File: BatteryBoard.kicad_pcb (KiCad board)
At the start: 4 copper layers, 124 parts, among them J1 Keystone-1042, J10 200528-0100, J2 Keystone-1042, J3 Keystone-1042, J4 Keystone-1042, J5 Keystone-1042, J6 Keystone-1042, J7 1824543, J8 Conn_01x06, Q1 NX3008NBKS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

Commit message: Repoured polys
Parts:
- moved U9 0.48 mm to (153.3, 98.5)
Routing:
- net SYSTEM_VDD: track 44.3 -> 36.3 mm
- net /Battery Bus Detection/CHARGE_EN: track 21.5 -> 20.7 mm
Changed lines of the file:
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@@
 	(footprint "Package_TO_SOT_SMD:TSOT-23-6"
 		(layer "B.Cu")
-		(at 153.3 98.01875 90)
+		(at 153.3 98.5 90)
 		(descr "TSOT, 6 Pin (https://www.jedec.org/sites/default/files/docs/MO-193D.pdf variant AA), generated with kicad-footprint-generator ipc_gullwing_generator.py")
 		(tags "TSOT TO_SOT_SMD")
@@
 	)
 	(segment
-		(start 154.25 96.88125)
-		(end 154.25 96.218751)
-		(width 0.381)
-		(layer "B.Cu")
-		(net 20)
-	)
-	(segment
 		(start 121.55 101.7125)
 		(end 121.8375 102)
@@
 	)
 	(segment
-		(start 154.25 96.218751)
-		(end 153.341999 95.31075)
-		(width 0.381)
-		(layer "B.Cu")
-		(net 20)
-	)
-	(segment
-		(start 149.299249 95.31075)
-		(end 147.885 96.724999)
-		(width 0.381)
-		(layer "B.Cu")
-		(net 20)
-	)
-	(segment
 		(start 121.5 114.0825)
 		(end 121.8375 114.42)
@@
 	)
 	(segment
-		(start 153.341999 95.31075)
-		(end 149.299249 95.31075)
-		(width 0.381)
-		(layer "B.Cu")
-		(net 20)
-	)
-	(segment
 		(start 121.55 98.25)
 		(end 121.55 101.7125)
@@
 	)
 	(segment
-		(start 150.051749 95.82825)
-		(end 153.07825 95.82825)
+		(start 153.3 97.20517)
+		(end 153.3 96.88125)
 		(width 0.254)
 		(layer "B.Cu")
@@
 	)
 	(segment
-		(start 153.07825 95.82825)
-		(end 153.3 96.05)
+		(start 153.3 97.68642)
+		(end 152.50517 98.48125)
 		(width 0.254)
 		(layer "B.Cu")
@@
 	)
 	(segment
-		(start 149.155 96.724999)
-		(end 150.051749 95.82825)
+		(start 152.50517 98.48125)
+		(end 150.911251 98.48125)
 		(width 0.254)
 		(layer "B.Cu")
@@
 	)
 	(segment
-		(start 153.3 96.05)
-		(end 153.3 96.88125)
+		(start 150.911251 98.48125)
+		(end 149.155 96.724999)
 		(width 0.254)
 		(layer "B.Cu")
@@
 	)
 	(segment
-		(start 144.825 107.825)
-		(end 143.5 107.825)
+		(start 155.614949 110.742999)
+		(end 145.742999 110.742999)
 		(width 0.254)
 		(layer "B.Cu")
@@
 	)
 	(segment
-		(start 143.75 107.825)
-		(end 143.075 107.825)
-		(width 0.381)
+		(start 143.5 108.5)
+		(end 143.5 107.825)
+		(width 0.254)
 		(layer "B.Cu")
 		(net 77)
 	)
 	(segment
-		(start 145.5 108.5)
-		(end 144.825 107.825)
+		(start 156.182949 110.174999)
+		(end 155.614949 110.742999)
 		(width 0.254)
 		(layer "B.Cu")
@@
 	)
 	(segment
-		(start 155.614949 110.742999)
-		(end 145.742999 110.742999)
-		(width 0.254)
-		(layer "B.Cu")
-		(net 77)
-	)
-	(segment
-		(start 145.5 110.5)
-		(end 145.5 108.5)
-		(width 0.254)
+		(start 143.75 107.825)
+		(end 143.075 107.825)
+		(width 0.381)
 		(layer "B.Cu")
 		(net 77)
@@
 	(segment
 		(start 145.742999 110.742999)
-		(end 145.5 110.5)
-		(width 0.254)
-		(layer "B.Cu")
-		(net 77)
-	)
-	(segment
-		(start 156.182949 110.174999)
-		(end 155.614949 110.742999)
+		(end 143.5 108.5)
 		(width 0.254)
 		(layer "B.Cu")
@@
 		(hatch edge 0.5)
 		(connect_pads yes
-			(clearance 0.254)
+			(clearance 0.5)
 		)
-		(min_thickness 0.254)
+		(min_thickness 0.5)
 		(filled_areas_thickness no)
 		(fill yes
@@
 			(pts
 				(xy 173.25 96) (xy 164.25 96) (xy 164.25 100.25) (xy 173.25 100.25) (xy 173.25 103) (xy 160 103)
-				(xy 154.5 98) (xy 154 98) (xy 154 96) (xy 153.341999 95.31075) (xy 149.299249 95.31075) (xy 147.885 97.419401)
+				(xy 154.5 98) (xy 153.75 98) (xy 153.75 96.75) (xy 150.25 96.75) (xy 149.905 96.8944) (xy 148.635 97.588802)
 				(xy 142.155 97.419401) (xy 137.75 97.5) (xy 137.75 95) (xy 140 92.75) (xy 173.25 92.75) (xy 173.25 93.25)
 			)

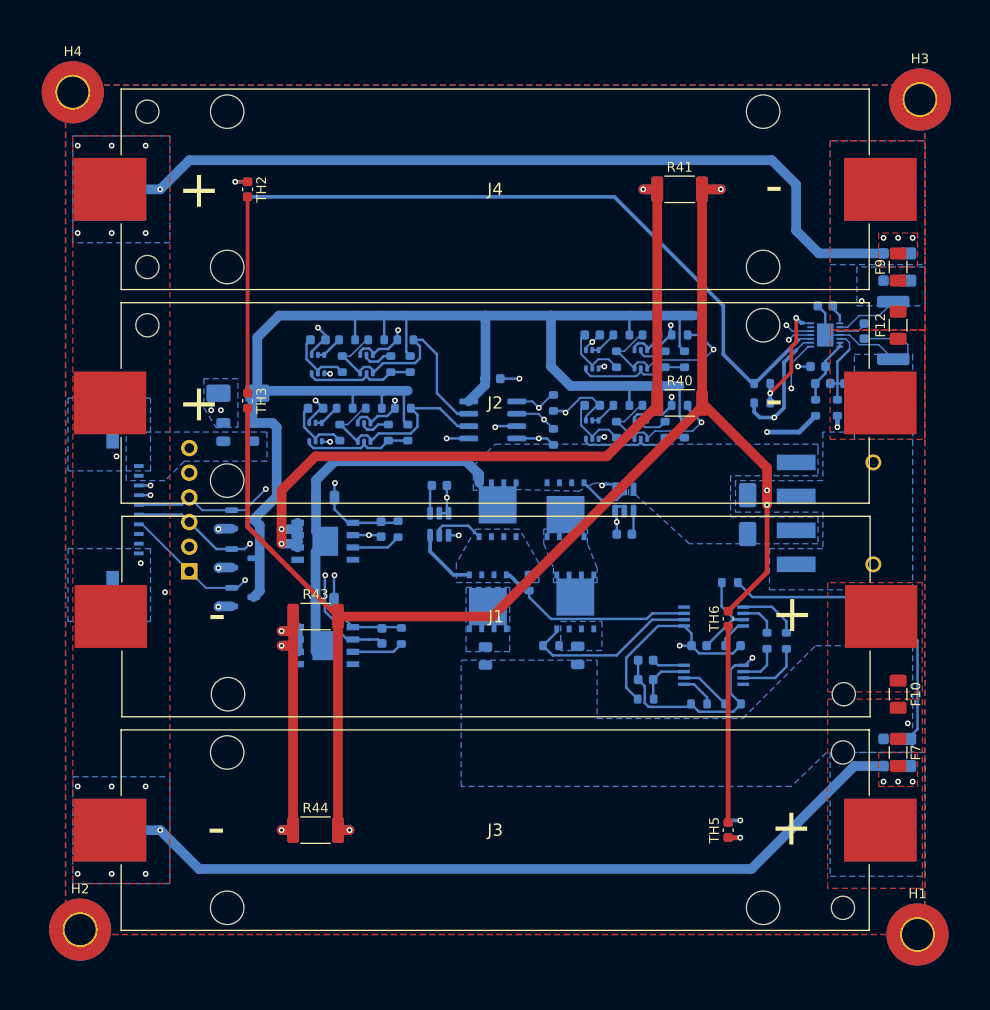
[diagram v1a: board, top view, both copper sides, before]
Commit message: Updated footprint to follow PC/104
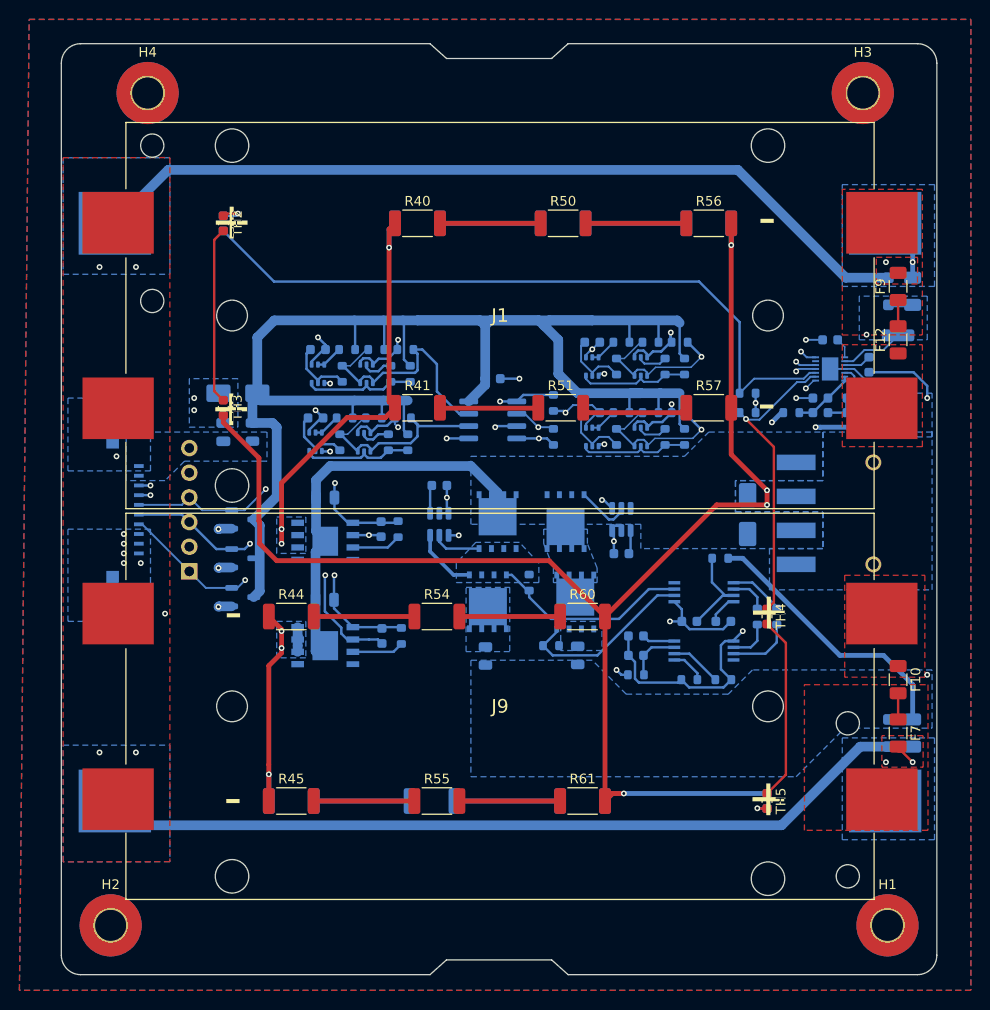
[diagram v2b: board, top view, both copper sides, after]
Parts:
- removed J2, J3, J4: Keystone-1042, Battery-Board:Keystone_1042
- removed NT1: NetTie_2, NetTie:NetTie-2_SMD_Pad2.0mm
- added J9: Keystone-1048, Battery-Board:BAT_1048, F.Cu at (140.5, 119.8)
- added R50: 160R, Resistor_SMD:R_2010_5025Metric, F.Cu at (147.0, 70.0)
- added R51: 160R, Resistor_SMD:R_2010_5025Metric, F.Cu at (146.8, 89.0)
- added R52: 160R, Resistor_SMD:R_2010_5025Metric, B.Cu at (147.0, 70.0)
- added R53: 160R, Resistor_SMD:R_2010_5025Metric, B.Cu at (133.5, 129.5)
- added R54: 160R, Resistor_SMD:R_2010_5025Metric, F.Cu at (134.0, 110.5)
- added R55: 160R, Resistor_SMD:R_2010_5025Metric, F.Cu at (134.0, 129.5)
- added R56: 160R, Resistor_SMD:R_2010_5025Metric, F.Cu at (162.0, 70.0)
- added R57: 160R, Resistor_SMD:R_2010_5025Metric, F.Cu at (162.0, 89.0)
- added R58: 160R, Resistor_SMD:R_2010_5025Metric, B.Cu at (162.0, 70.0)
- added R59: 160R, Resistor_SMD:R_2010_5025Metric, B.Cu at (149.0, 129.5)
- added R60: 160R, Resistor_SMD:R_2010_5025Metric, F.Cu at (149.0, 110.5)
- added R61: 160R, Resistor_SMD:R_2010_5025Metric, F.Cu at (149.0, 129.5)
- J1: value Keystone-1042 -> Keystone-1048; footprint Battery-Board:Keystone_1042 -> Battery-Board:BAT_1048
- R40, R41, R42, R44: value 470R -> 160R
- R43: value 470R -> 160R; moved to B.Cu
- R45: value 470R -> 160R; moved to F.Cu
- TH4: moved to F.Cu
- TH6: moved to B.Cu
- moved R41 35.1 mm to (132.0, 89.0)
- moved R40 32.7 mm to (132.0, 70.0)
- moved J1 31.0 mm to (140.5, 79.5), turned to 180 degrees
- moved R42 27.2 mm to (132.0, 70.0)
- moved TH4 22.4 mm to (168.0, 110.5)
- moved R44 22.1 mm to (119.0, 110.5)
- moved TH6 19.2 mm to (168.0, 129.5)
- moved R43 19.2 mm to (119.0, 129.5)
- moved H4 7.71 mm to (104.2, 56.6)
- moved H3 5.92 mm to (177.9, 56.6)
- moved TH5 5.00 mm to (168.0, 129.5), turned to -90 degrees
- moved TH1 4.30 mm to (112.0, 70.0)
- moved TH2 4.30 mm to (112.0, 70.0)
- moved R45 3.91 mm to (119.0, 129.5)
- moved C8 3.54 mm to (174.5, 82.0)
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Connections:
- C7 pad 2: /Battery Monitor/CSN -> SYSTEM_VSS
- C8 pad 2: /Battery Monitor/CSN -> SYSTEM_VSS
- C9 pad 2: /Battery Monitor/CSN -> SYSTEM_VSS
- F10 pad 1: Net-(J1-POS) -> Net-(F10-Pad1)
- F12 pad 1: Net-(J2-NEG) -> Net-(F12-Pad1)
- F12 pad 2: Net-(J4-NEG) -> Net-(F12-Pad2)
- F9 pad 1: Net-(J4-NEG) -> Net-(F12-Pad2)
- J1 pad 1: /Battery/BATT1 -> Net-(F12-Pad1)
- J1 pad 2: Net-(J1-POS) -> /Battery/BATT1
- J10 pad 2: unconnected-(J10-Pin_2-Pad2) -> GND
- J10 pad 3: unconnected-(J10-Pin_3-Pad3) -> GND
- R40 pad 2: SYSTEM_VSS -> Net-(R40-Pad2)
- R41 pad 2: SYSTEM_VSS -> Net-(R41-Pad2)
- R42 pad 2: SYSTEM_VSS -> Net-(R42-Pad2)
- R43 pad 2: SYSTEM_VSS -> Net-(R43-Pad2)
- R44 pad 2: SYSTEM_VSS -> Net-(R44-Pad2)
- R45 pad 2: SYSTEM_VSS -> Net-(R45-Pad2)
- R9 pad 1: /Battery Monitor/CSN -> SYSTEM_VSS
- U3 pad 15: /Battery Monitor/CSN -> SYSTEM_VSS
- U3 pad 4: /Battery Monitor/CSN -> SYSTEM_VSS
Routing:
- net /Battery Temperature Protection/HEATER: track 78.9 -> 43.4 mm
- net SYSTEM_VSS: track 148.8 -> 182.9 mm, vias 4 -> 6
- net /Battery Monitor/THERM1: track 57.3 -> 31.0 mm, vias 2 -> 1
- net Net-(TH5-Pad2): track 20.2 -> 2.02 mm, vias 0 -> 1
- net /Battery Monitor/CSN: track 18.1 -> 0.00 mm
- net Net-(TH4-Pad2): track 2.50 -> 19.1 mm, vias 1 -> 0
- net +3V3: track 156.3 -> 172.3 mm
- net Net-(R51-Pad2): track 0.00 -> 11.0 mm
- net Net-(R53-Pad2): track 0.00 -> 10.9 mm
- net Net-(R55-Pad2): track 0.00 -> 10.4 mm
- net Net-(R54-Pad2): track 0.00 -> 10.4 mm
- net Net-(R52-Pad2): track 0.00 -> 10.4 mm
- net Net-(R50-Pad2): track 0.00 -> 10.4 mm
- net Net-(R45-Pad2): track 0.00 -> 10.4 mm
- net Net-(R44-Pad2): track 0.00 -> 10.4 mm
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- added copper zone on B.Cu, net /Battery Temperature Protection/HEATER
- added copper zone on B.Cu, net /Battery Temperature Protection1/HEATER
- added copper zone on F.Cu, net Net-(F10-Pad1)
- added copper zone on F.Cu, net Net-(F12-Pad1)
- added copper zone on F.Cu, net Net-(F12-Pad2)
- removed copper zone on B.Cu, net /Battery Monitor/CSN
- removed copper zone on F.Cu, net Net-(J1-POS)
- removed copper zone on F.Cu, net Net-(J2-NEG)
- removed copper zone on F.Cu, net Net-(J4-NEG)
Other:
- board outline added: 90.2 x 95.9 mm
